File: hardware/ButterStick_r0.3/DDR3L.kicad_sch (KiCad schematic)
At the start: 2 parts, among them U5 MT41K64M16TW-107_J-TR

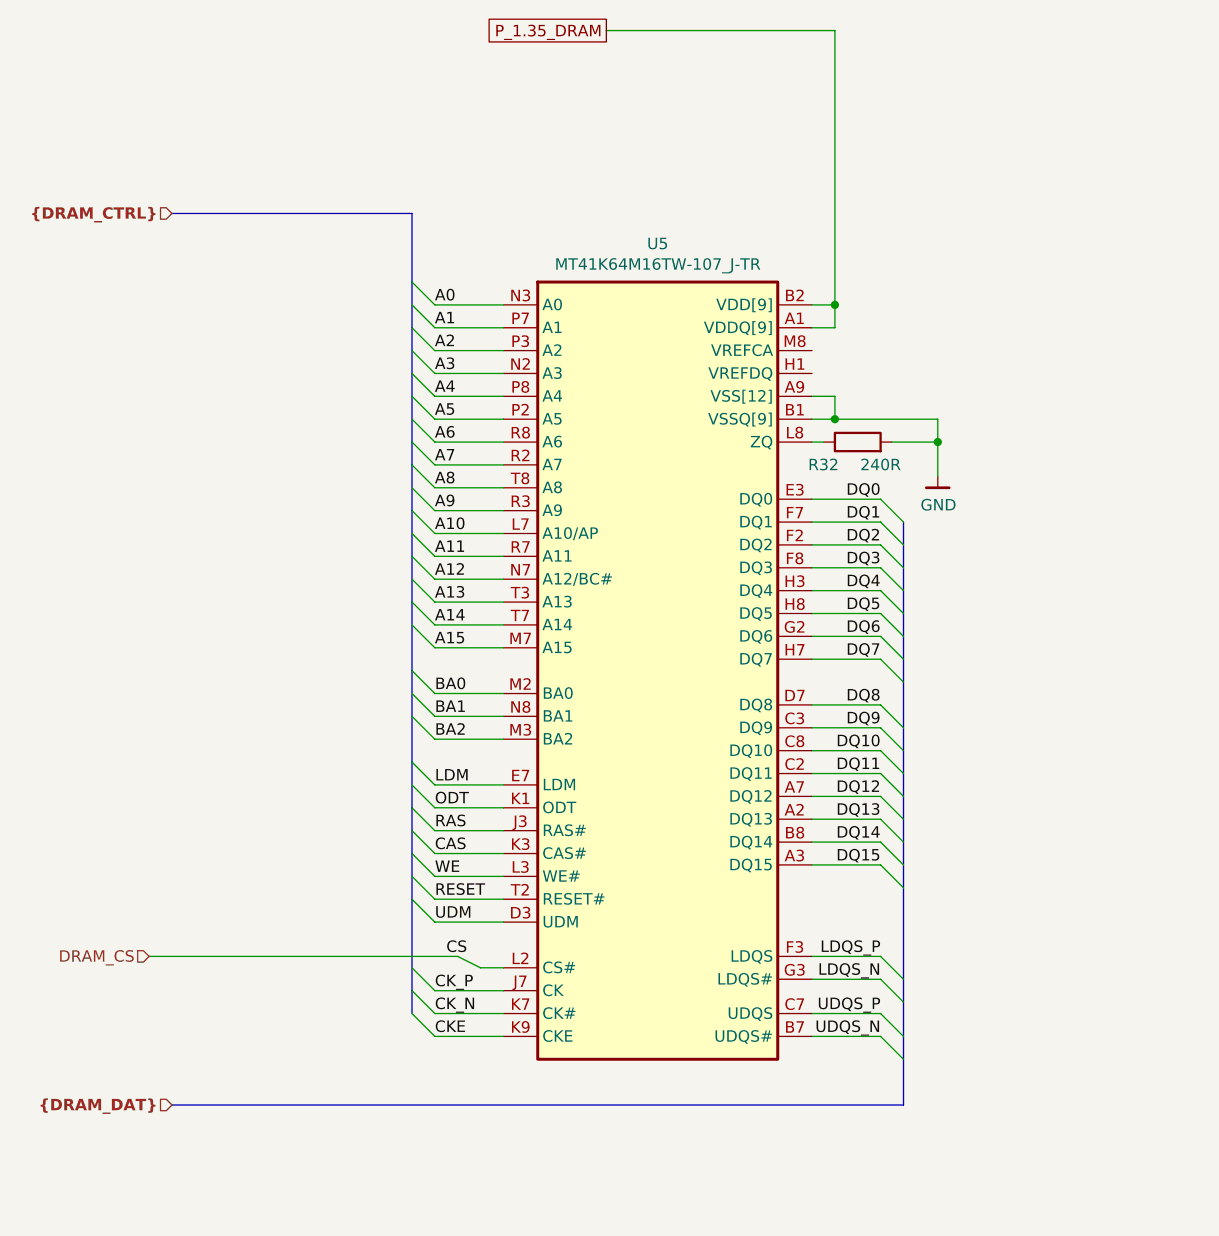
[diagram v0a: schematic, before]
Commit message: hw.r0_3: routing improvements
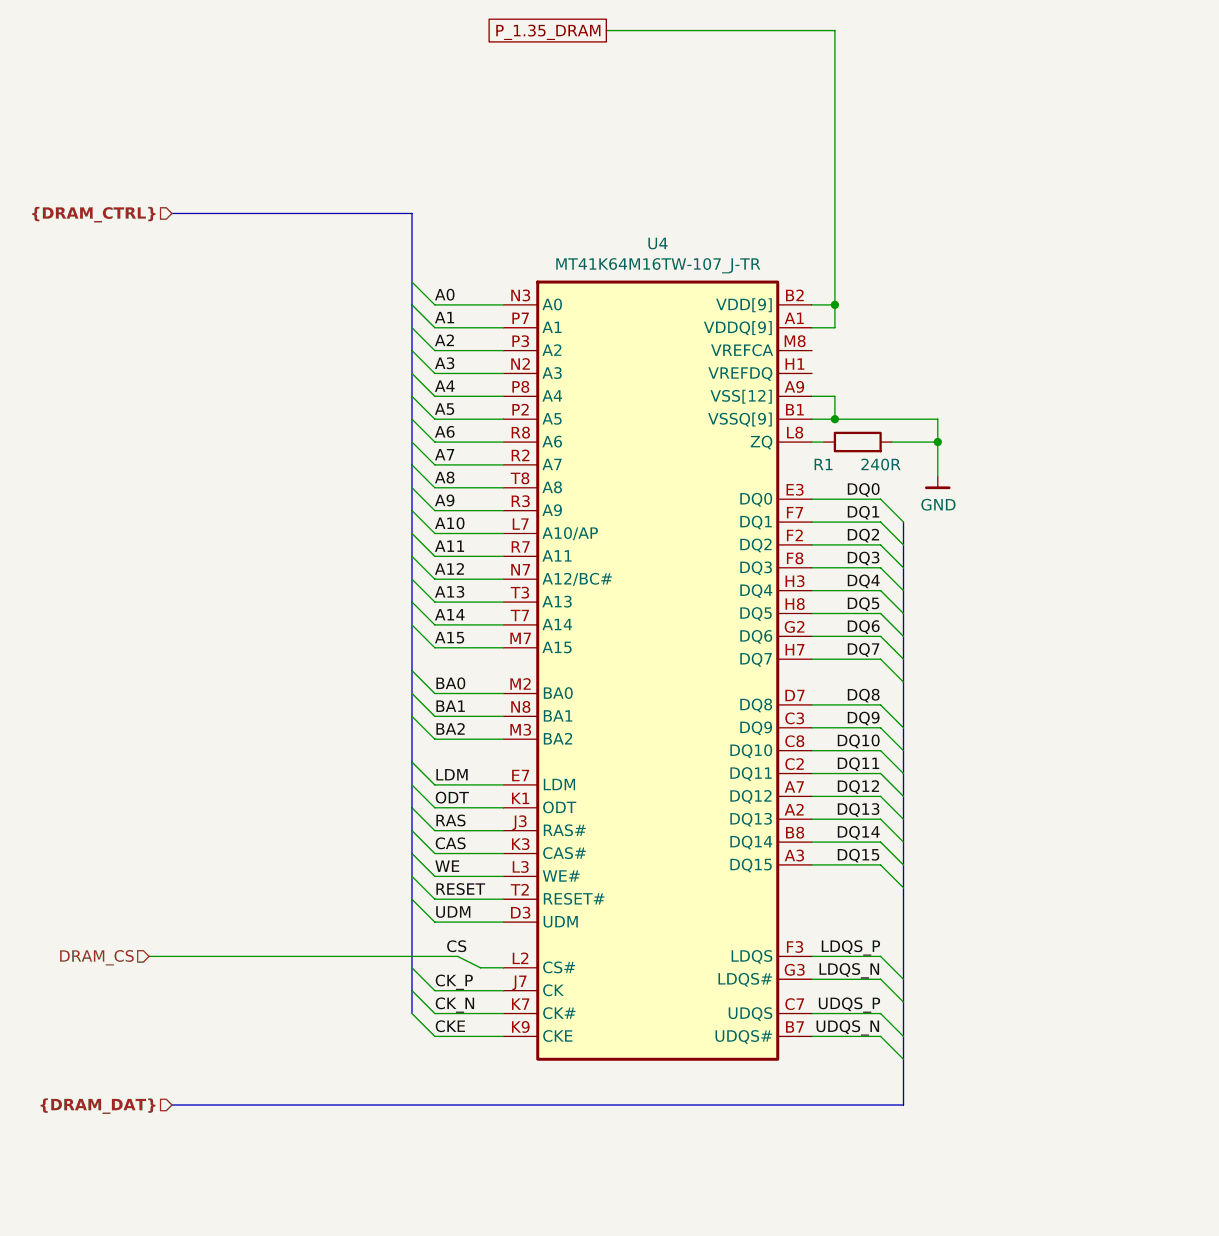
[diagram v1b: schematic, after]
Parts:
- renumbered R32 to R1, U5 to U4
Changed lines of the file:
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@@
 (kicad_sch (version 20200512) (host eeschema "5.99.0-unknown-c8476d6~101~ubuntu18.04.1")
-  (page 14 20)
+  (page 1 20)
   (paper "A4")
   (junction (at 157.48 66.04))
@@
   (bus (pts (xy 83.82 55.88) (xy 110.49 55.88)))
   (bus (pts (xy 83.82 154.94) (xy 165.1 154.94)))
-  (bus (pts (xy 110.49 55.88) (xy 110.49 63.5)))
-  (bus (pts (xy 110.49 63.5) (xy 110.49 68.58)))
-  (bus (pts (xy 110.49 68.58) (xy 110.49 73.66)))
-  (bus (pts (xy 110.49 73.66) (xy 110.49 76.2)))
-  (bus (pts (xy 110.49 76.2) (xy 110.49 81.28)))
-  (bus (pts (xy 110.49 81.28) (xy 110.49 83.82)))
+  (bus (pts (xy 110.49 55.88) (xy 110.49 66.04)))
+  (bus (pts (xy 110.49 66.04) (xy 110.49 71.12)))
+  (bus (pts (xy 110.49 71.12) (xy 110.49 76.2)))
+  (bus (pts (xy 110.49 76.2) (xy 110.49 78.74)))
+  (bus (pts (xy 110.49 78.74) (xy 110.49 83.82)))
   (bus (pts (xy 110.49 83.82) (xy 110.49 88.9)))
   (bus (pts (xy 110.49 88.9) (xy 110.49 93.98)))
@@
   (bus (pts (xy 165.1 107.95) (xy 165.1 113.03)))
   (bus (pts (xy 165.1 113.03) (xy 165.1 118.11)))
-  (bus (pts (xy 165.1 118.11) (xy 165.1 120.65)))
-  (bus (pts (xy 165.1 120.65) (xy 165.1 125.73)))
-  (bus (pts (xy 165.1 125.73) (xy 165.1 130.81)))
-  (bus (pts (xy 165.1 130.81) (xy 165.1 143.51)))
+  (bus (pts (xy 165.1 118.11) (xy 165.1 123.19)))
+  (bus (pts (xy 165.1 123.19) (xy 165.1 128.27)))
+  (bus (pts (xy 165.1 128.27) (xy 165.1 140.97)))
+  (bus (pts (xy 165.1 140.97) (xy 165.1 143.51)))
   (bus (pts (xy 165.1 143.51) (xy 165.1 149.86)))
   (bus (pts (xy 165.1 149.86) (xy 165.1 154.94)))
@@
   )
   (symbol (lib_id "power:GND") (at 168.91 85.09 0)
-    (property "Reference" "#PWR0108" (id 0) (at 168.91 91.44 0)
+    (property "Reference" "#PWR0224" (id 0) (at 168.91 91.44 0)
       (effects (font (size 1.27 1.27)) hide)
     )
@@
   )
   (symbol (lib_id "Device:R") (at 160.02 81.28 90)
-    (property "Reference" "R32" (id 0) (at 156.21 83.82 90))
+    (property "Reference" "R1" (id 0) (at 156.21 83.82 90))
     (property "Value" "240R" (id 1) (at 162.56 83.82 90))
     (property "Footprint" "" (id 2) (at 160.02 83.058 90)
@@
   )
   (symbol (lib_id "gkl_mem:MT41K512M16TW") (at 137.16 96.52 0)
-    (property "Reference" "U5" (id 0) (at 137.795 59.2582 0))
+    (property "Reference" "U4" (id 0) (at 137.795 59.2582 0))
     (property "Value" "MT41K64M16TW-107_J-TR" (id 1) (at 137.795 61.5442 0))
     (property "Footprint" "Package_BGA:BGA-96_9.0x13.0mm_Layout2x3x16_P0.8mm" (id 2) (at 138.43 58.42 0)

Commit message: hw.r0_3: Start routing DDR3 interface
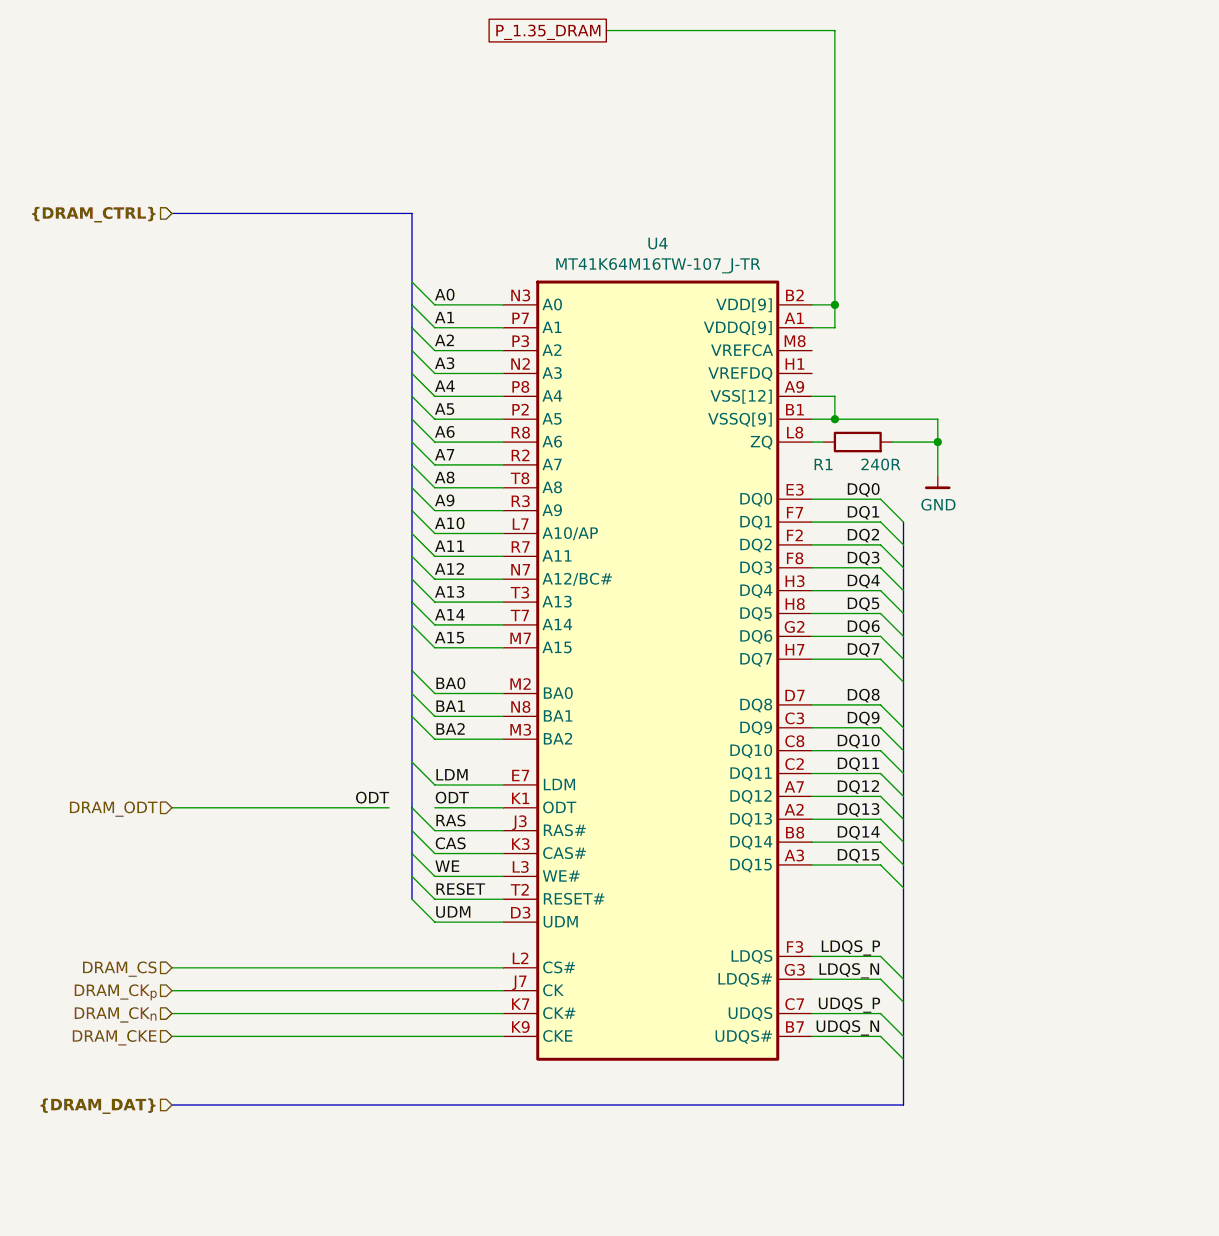
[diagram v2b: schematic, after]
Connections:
- net CKE renamed DRAM_CKE
- net CK_N renamed DRAM_CK_{n}
- net CK_P renamed DRAM_CK_{p}
- net ODT renamed DRAM_ODT
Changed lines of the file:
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@@
-(kicad_sch (version 20200512) (host eeschema "5.99.0-unknown-c8476d6~101~ubuntu18.04.1")
+(kicad_sch (version 20200512) (host eeschema "5.99.0-unknown-711fc99~101~ubuntu18.04.1")
   (page 1 20)
   (paper "A4")
@@
   (bus_entry (at 110.49 111.76) (size 2.54 2.54))
   (bus_entry (at 110.49 116.84) (size 2.54 2.54))
-  (bus_entry (at 110.49 119.38) (size 2.54 2.54))
   (bus_entry (at 110.49 121.92) (size 2.54 2.54))
   (bus_entry (at 110.49 124.46) (size 2.54 2.54))
@@
   (bus_entry (at 110.49 129.54) (size 2.54 2.54))
   (bus_entry (at 110.49 132.08) (size 2.54 2.54))
-  (bus_entry (at 110.49 139.7) (size 2.54 2.54))
-  (bus_entry (at 110.49 142.24) (size 2.54 2.54))
-  (bus_entry (at 110.49 144.78) (size 2.54 2.54))
   (bus_entry (at 165.1 90.17) (size -2.54 -2.54))
   (bus_entry (at 165.1 92.71) (size -2.54 -2.54))
@@
   (bus_entry (at 165.1 147.32) (size -2.54 -2.54))
   (bus_entry (at 165.1 149.86) (size -2.54 -2.54))
-  (wire (pts (xy 81.28 138.43) (xy 115.57 138.43)))
+  (wire (pts (xy 83.82 121.92) (xy 107.95 121.92)))
+  (wire (pts (xy 83.82 139.7) (xy 120.65 139.7)))
+  (wire (pts (xy 83.82 142.24) (xy 120.65 142.24)))
+  (wire (pts (xy 83.82 144.78) (xy 120.65 144.78)))
+  (wire (pts (xy 83.82 147.32) (xy 120.65 147.32)))
   (wire (pts (xy 113.03 66.04) (xy 120.65 66.04)))
   (wire (pts (xy 113.03 68.58) (xy 120.65 68.58)))
@@
   (wire (pts (xy 113.03 132.08) (xy 120.65 132.08)))
   (wire (pts (xy 113.03 134.62) (xy 120.65 134.62)))
-  (wire (pts (xy 113.03 142.24) (xy 120.65 142.24)))
-  (wire (pts (xy 113.03 144.78) (xy 120.65 144.78)))
-  (wire (pts (xy 113.03 147.32) (xy 120.65 147.32)))
-  (wire (pts (xy 115.57 138.43) (xy 118.11 139.7)))
-  (wire (pts (xy 118.11 139.7) (xy 120.65 139.7)))
   (wire (pts (xy 154.94 66.04) (xy 157.48 66.04)))
   (wire (pts (xy 154.94 68.58) (xy 157.48 68.58)))
@@
   (bus (pts (xy 83.82 154.94) (xy 165.1 154.94)))
   (bus (pts (xy 110.49 55.88) (xy 110.49 66.04)))
-  (bus (pts (xy 110.49 66.04) (xy 110.49 71.12)))
-  (bus (pts (xy 110.49 71.12) (xy 110.49 76.2)))
-  (bus (pts (xy 110.49 76.2) (xy 110.49 78.74)))
+  (bus (pts (xy 110.49 66.04) (xy 110.49 68.58)))
+  (bus (pts (xy 110.49 68.58) (xy 110.49 73.66)))
+  (bus (pts (xy 110.49 73.66) (xy 110.49 78.74)))
   (bus (pts (xy 110.49 78.74) (xy 110.49 83.82)))
   (bus (pts (xy 110.49 83.82) (xy 110.49 88.9)))
@@
   (bus (pts (xy 110.49 99.06) (xy 110.49 106.68)))
   (bus (pts (xy 110.49 106.68) (xy 110.49 111.76)))
-  (bus (pts (xy 110.49 111.76) (xy 110.49 116.84)))
-  (bus (pts (xy 110.49 116.84) (xy 110.49 121.92)))
+  (bus (pts (xy 110.49 111.76) (xy 110.49 121.92)))
   (bus (pts (xy 110.49 121.92) (xy 110.49 127)))
   (bus (pts (xy 110.49 127) (xy 110.49 132.08)))
-  (bus (pts (xy 110.49 132.08) (xy 110.49 142.24)))
-  (bus (pts (xy 110.49 142.24) (xy 110.49 144.78)))
   (bus (pts (xy 165.1 90.17) (xy 165.1 95.25)))
   (bus (pts (xy 165.1 95.25) (xy 165.1 100.33)))
   (bus (pts (xy 165.1 100.33) (xy 165.1 102.87)))
   (bus (pts (xy 165.1 102.87) (xy 165.1 107.95)))
-  (bus (pts (xy 165.1 107.95) (xy 165.1 113.03)))
-  (bus (pts (xy 165.1 113.03) (xy 165.1 118.11)))
-  (bus (pts (xy 165.1 118.11) (xy 165.1 123.19)))
-  (bus (pts (xy 165.1 123.19) (xy 165.1 128.27)))
-  (bus (pts (xy 165.1 128.27) (xy 165.1 140.97)))
-  (bus (pts (xy 165.1 140.97) (xy 165.1 143.51)))
+  (bus (pts (xy 165.1 107.95) (xy 165.1 115.57)))
+  (bus (pts (xy 165.1 115.57) (xy 165.1 120.65)))
+  (bus (pts (xy 165.1 120.65) (xy 165.1 125.73)))
+  (bus (pts (xy 165.1 125.73) (xy 165.1 130.81)))
+  (bus (pts (xy 165.1 130.81) (xy 165.1 143.51)))
   (bus (pts (xy 165.1 143.51) (xy 165.1 149.86)))
   (bus (pts (xy 165.1 149.86) (xy 165.1 154.94)))
+  (label "ODT" (at 107.95 121.92 180)
+    (effects (font (size 1.27 1.27)) (justify right bottom))
+  )
   (label "A0" (at 113.03 66.04 0)
     (effects (font (size 1.27 1.27)) (justify left bottom))
@@
     (effects (font (size 1.27 1.27)) (justify left bottom))
   )
-  (label "CK_P" (at 113.03 142.24 0)
-    (effects (font (size 1.27 1.27)) (justify left bottom))
-  )
-  (label "CK_N" (at 113.03 144.78 0)
-    (effects (font (size 1.27 1.27)) (justify left bottom))
-  )
-  (label "CKE" (at 113.03 147.32 0)
-    (effects (font (size 1.27 1.27)) (justify left bottom))
-  )
-  (label "CS" (at 114.3 138.43 0)
-    (effects (font (size 1.27 1.27)) (justify left bottom))
-  )
   (label "DQ0" (at 162.56 87.63 180)
     (effects (font (size 1.27 1.27)) (justify right bottom))
@@
   )
   (global_label "P_1.35_DRAM" (shape passive) (at 132.08 35.56 180)
-    (effects (font (size 1.27 1.27)) (justify right))
-  )
-  (hierarchical_label "DRAM_CS" (shape input) (at 81.28 138.43 180)
     (effects (font (size 1.27 1.27)) (justify right))
   )
@@
     (effects (font (size 1.27 1.27) (thickness 0.254) bold) (justify right))
   )
+  (hierarchical_label "DRAM_ODT" (shape input) (at 83.82 121.92 180)
+    (effects (font (size 1.27 1.27)) (justify right))
+  )
+  (hierarchical_label "DRAM_CS" (shape input) (at 83.82 139.7 180)
+    (effects (font (size 1.27 1.27)) (justify right))
+  )
+  (hierarchical_label "DRAM_CK_{p}" (shape input) (at 83.82 142.24 180)
+    (effects (font (size 1.27 1.27)) (justify right))
+  )
+  (hierarchical_label "DRAM_CK_{n}" (shape input) (at 83.82 144.78 180)
+    (effects (font (size 1.27 1.27)) (justify right))
+  )
+  (hierarchical_label "DRAM_CKE" (shape input) (at 83.82 147.32 180)
+    (effects (font (size 1.27 1.27)) (justify right))
+  )
   (hierarchical_label "{DRAM_DAT}" (shape input) (at 83.82 154.94 180)
